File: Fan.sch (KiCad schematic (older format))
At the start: 0 parts

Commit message: Fan Schematic
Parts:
- added Q?: MOSFET_N, ~, symbol MOSFET_N
- added R? (x5): R, ~, symbol R
- added RV?: POT, ~, symbol POT
- added U?: LM324, ~, symbol LM324
- added U?: MCP4922-E/P, DIP14, symbol MCP4922-E/P
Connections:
- net labels added: +12V, -12V, AGND, CS_N, Current Measure, MISO, MOSI, SCLK
- wire segments 0 -> 35

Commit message: Overall Schematic
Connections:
- net labels added: CURR_MEAS, FAN_EN_N, FAN_OUT+, FAN_OUT-, TACH_IN, TACH_MEAS
- net labels removed: Current Measure, Fan_In, Power+, Power-, Tach, Tach_Out
- wire segments 35 -> 43
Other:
- moved on the sheet: R?
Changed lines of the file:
@@
 $Descr A4 11693 8268
 encoding utf-8
-Sheet 7 9
+Sheet 5 9
 Title ""
-Date "22 sep 2013"
+Date "28 sep 2013"
 Rev ""
 Comp ""
@@
 $EndDescr
 Text HLabel 2550 2950 0    60   Input ~ 0
-Fan_In
+FAN_EN_N
 Text HLabel 2550 3200 0    60   Output ~ 0
-Tach_Out
+TACH_MEAS
 Text HLabel 8950 2450 0    60   Output ~ 0
-Power+
-Text HLabel 8950 2650 0    60   Input ~ 0
-Power-
+FAN_OUT+
+Text HLabel 8950 2650 0    60   Output ~ 0
+FAN_OUT-
 Text HLabel 8950 2850 0    60   Input ~ 0
-Tach
+TACH_IN
 $Comp
 L LM324 U?
@@
 	8950 2650 7600 2650
 Wire Wire Line
-	7600 2650 7600 3300
+	7600 2650 7600 3200
+Wire Wire Line
+	7600 3200 7600 3300
 $Comp
 L R R?
@@
 	5950 2850 5950 2550
 Wire Wire Line
-	3500 3200 7600 3200
+	3500 3200 5350 3200
+Wire Wire Line
+	5350 3200 7600 3200
 Wire Wire Line
 	5350 3200 5350 2250
@@
 	7600 1950 7600 1550
 Wire Wire Line
-	4200 2050 5550 2050
+	4250 2050 4700 2050
+Wire Wire Line
+	4700 2050 5550 2050
 $Comp
 L +12V #PWR?
@@
 	4250 1500 4250 1250
 Wire Wire Line
-	4250 2000 4250 2300
+	4250 2000 4250 2050
+Wire Wire Line
+	4250 2050 4250 2150
+Wire Wire Line
+	4250 2150 4250 2300
 $Comp
 L POT RV?
@@
 Wire Wire Line
 	3150 3200 2550 3200
-Text HLabel 2850 3100 0    60   Output ~ 0
-Current Measure
+Text HLabel 2600 3100 0    60   Output ~ 0
+CURR_MEAS
 Wire Wire Line
 	3500 3200 3500 3100
 Wire Wire Line
-	3500 3100 2850 3100
+	3500 3100 2600 3100
 Connection ~ 5350 3200
 Wire Wire Line
-	2550 2950 3600 2950
+	2550 2950 2850 2950
+Wire Wire Line
+	2850 2950 3600 2950
 Wire Wire Line
 	3600 2950 3600 3150
@@
 L R R?
 U 1 1 523BCB9D
-P 3950 2050
-F 0 "R?" V 4030 2050 40  0000 C CNN
-F 1 "R" V 3957 2051 40  0000 C CNN
-F 2 "~" V 3880 2050 30  0000 C CNN
-F 3 "~" H 3950 2050 30  0000 C CNN
-	1    3950 2050
+P 3900 2100
+F 0 "R?" V 3980 2100 40  0000 C CNN
+F 1 "R" V 3907 2101 40  0000 C CNN
+F 2 "~" V 3830 2100 30  0000 C CNN
+F 3 "~" H 3900 2100 30  0000 C CNN
+	1    3900 2100
 	0    -1   -1   0
 $EndComp
 Wire Wire Line
-	3650 2050 3700 2050
+	3650 2050 3650 2100
 Text HLabel 2200 2000 0    60   Input ~ 0
 MOSI
@@
 	2850 2750 2850 2950
 Connection ~ 2850 2950
+Wire Wire Line
+	4150 2150 4250 2150
+Wire Wire Line
+	4150 2150 4150 2100
+Connection ~ 4250 2150
 $EndSCHEMATC

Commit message: Fan/Current Module Refactoring
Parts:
- removed R? (x3): R, ~, symbol R
- removed RV?: POT, ~, symbol POT
- added D?: DIODE, ~, symbol DIODE
- added Q? (x2): MOSFET_N, ~, symbol MOSFET_N
- added TH?: THERMISTOR, ~, symbol THERMISTOR
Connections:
- net labels added: +12C, FAN_MODE, FAN_PWM
- net labels removed: FAN_EN_N
- wire segments 43 -> 30
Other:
- moved on the sheet: R?
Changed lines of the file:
@@
 Sheet 5 9
 Title ""
-Date "28 sep 2013"
+Date "30 sep 2013"
 Rev ""
 Comp ""
@@
 Comment4 ""
 $EndDescr
-Text HLabel 2550 2950 0    60   Input ~ 0
-FAN_EN_N
-Text HLabel 2550 3200 0    60   Output ~ 0
+Text HLabel 2600 2950 0    60   Input ~ 0
+FAN_PWM
+Text HLabel 2600 4450 0    60   Output ~ 0
 TACH_MEAS
-Text HLabel 8950 2450 0    60   Output ~ 0
+Text HLabel 9300 1450 2    60   Output ~ 0
 FAN_OUT+
-Text HLabel 8950 2650 0    60   Output ~ 0
+Text HLabel 9300 1650 2    60   Output ~ 0
 FAN_OUT-
-Text HLabel 8950 2850 0    60   Input ~ 0
+Text HLabel 9250 4450 2    60   Input ~ 0
 TACH_IN
 $Comp
@@
 	1    0    0    -1
 $EndComp
-$Comp
-L +12V #PWR?
-U 1 1 523BC5F8
-P 7600 1600
-F 0 "#PWR?" H 7600 1550 20  0001 C CNN
-F 1 "+12V" H 7600 1700 30  0000 C CNN
-F 2 "" H 7600 1600 60  0000 C CNN
-F 3 "" H 7600 1600 60  0000 C CNN
-	1    7600 1600
-	1    0    0    -1
-$EndComp
 Wire Wire Line
 	6550 2150 7300 2150
 Wire Wire Line
-	7600 2350 7600 2450
-Wire Wire Line
-	7600 2450 8950 2450
-Wire Wire Line
-	8950 2650 7600 2650
-Wire Wire Line
-	7600 2650 7600 3200
-Wire Wire Line
-	7600 3200 7600 3300
+	7600 2350 7600 3450
 $Comp
 L R R?
 U 1 1 523BC667
-P 7600 3550
-F 0 "R?" V 7680 3550 40  0000 C CNN
-F 1 "R" V 7607 3551 40  0000 C CNN
-F 2 "~" V 7530 3550 30  0000 C CNN
-F 3 "~" H 7600 3550 30  0000 C CNN
-	1    7600 3550
+P 7600 3700
+F 0 "R?" V 7680 3700 40  0000 C CNN
+F 1 "R" V 7607 3701 40  0000 C CNN
+F 2 "~" V 7530 3700 30  0000 C CNN
+F 3 "~" H 7600 3700 30  0000 C CNN
+	1    7600 3700
 	1    0    0    -1
 $EndComp
@@
 L AGND #PWR?
 U 1 1 523BC6A2
-P 7600 4050
-F 0 "#PWR?" H 7600 4050 40  0001 C CNN
-F 1 "AGND" H 7600 3980 50  0000 C CNN
-F 2 "" H 7600 4050 60  0000 C CNN
-F 3 "" H 7600 4050 60  0000 C CNN
-	1    7600 4050
-	1    0    0    -1
-$EndComp
-Wire Wire Line
-	7600 3800 7600 4050
+P 7600 4250
+F 0 "#PWR?" H 7600 4250 40  0001 C CNN
+F 1 "AGND" H 7600 4180 50  0000 C CNN
+F 2 "" H 7600 4250 60  0000 C CNN
+F 3 "" H 7600 4250 60  0000 C CNN
+	1    7600 4250
+	1    0    0    -1
+$EndComp
+Wire Wire Line
+	7600 3950 7600 4250
 $Comp
 L +12V #PWR?
@@
 	5950 2850 5950 2550
 Wire Wire Line
-	3500 3200 5350 3200
-Wire Wire Line
-	5350 3200 7600 3200
+	2600 3200 7600 3200
 Wire Wire Line
 	5350 3200 5350 2250
@@
 Connection ~ 7600 3200
 Wire Wire Line
-	7600 1950 7600 1550
-Wire Wire Line
-	4250 2050 4700 2050
-Wire Wire Line
-	4700 2050 5550 2050
-$Comp
-L +12V #PWR?
-U 1 1 523BC77F
-P 4250 1250
-F 0 "#PWR?" H 4250 1200 20  0001 C CNN
-F 1 "+12V" H 4250 1350 30  0000 C CNN
-F 2 "" H 4250 1250 60  0000 C CNN
-F 3 "" H 4250 1250 60  0000 C CNN
-	1    4250 1250
-	1    0    0    -1
-$EndComp
-$Comp
-L R R?
-U 1 1 523BC78E
-P 4250 1750
-F 0 "R?" V 4330 1750 40  0000 C CNN
-F 1 "R" V 4257 1751 40  0000 C CNN
-F 2 "~" V 4180 1750 30  0000 C CNN
-F 3 "~" H 4250 1750 30  0000 C CNN
-	1    4250 1750
-	1    0    0    -1
-$EndComp
-Wire Wire Line
-	4250 1500 4250 1250
-Wire Wire Line
-	4250 2000 4250 2050
-Wire Wire Line
-	4250 2050 4250 2150
-Wire Wire Line
-	4250 2150 4250 2300
-$Comp
-L POT RV?
-U 1 1 523BC7D3
-P 4250 2550
-F 0 "RV?" H 4250 2450 50  0000 C CNN
-F 1 "POT" H 4250 2550 50  0000 C CNN
-F 2 "~" H 4250 2550 60  0000 C CNN
-F 3 "~" H 4250 2550 60  0000 C CNN
-	1    4250 2550
-	0    -1   -1   0
-$EndComp
-Connection ~ 4250 2050
-Wire Wire Line
-	4250 2950 4250 2800
+	4150 2050 5550 2050
+Wire Wire Line
+	4250 2750 4250 2950
 $Comp
 L AGND #PWR?
@@
 	1    0    0    -1
 $EndComp
-Wire Wire Line
-	8950 2850 8250 2850
-Wire Wire Line
-	8250 2850 8250 4200
-Wire Wire Line
-	8250 4200 3150 4200
-Wire Wire Line
-	3150 4200 3150 3200
-Wire Wire Line
-	3150 3200 2550 3200
-Text HLabel 2600 3100 0    60   Output ~ 0
+Text HLabel 2600 3200 0    60   Output ~ 0
 CURR_MEAS
-Wire Wire Line
-	3500 3200 3500 3100
-Wire Wire Line
-	3500 3100 2600 3100
 Connection ~ 5350 3200
 Wire Wire Line
-	2550 2950 2850 2950
-Wire Wire Line
-	2850 2950 3600 2950
-Wire Wire Line
-	3600 2950 3600 3150
-Wire Wire Line
-	3600 3150 4700 3150
-Connection ~ 4700 2050
-$Comp
-L R R?
-U 1 1 523BCA8F
-P 4700 2550
-F 0 "R?" V 4780 2550 40  0000 C CNN
-F 1 "R" V 4707 2551 40  0000 C CNN
-F 2 "~" V 4630 2550 30  0000 C CNN
-F 3 "~" H 4700 2550 30  0000 C CNN
-	1    4700 2550
-	1    0    0    -1
-$EndComp
-Wire Wire Line
-	4700 3150 4700 2800
-Wire Wire Line
-	4700 2300 4700 2050
+	2600 2950 3600 2950
 $Comp
 L R R?
 U 1 1 523BCB9D
-P 3900 2100
-F 0 "R?" V 3980 2100 40  0000 C CNN
-F 1 "R" V 3907 2101 40  0000 C CNN
-F 2 "~" V 3830 2100 30  0000 C CNN
-F 3 "~" H 3900 2100 30  0000 C CNN
-	1    3900 2100
+P 3900 2050
+F 0 "R?" V 3980 2050 40  0000 C CNN
+F 1 "R" V 3907 2051 40  0000 C CNN
+F 2 "~" V 3830 2050 30  0000 C CNN
+F 3 "~" H 3900 2050 30  0000 C CNN
+	1    3900 2050
 	0    -1   -1   0
 $EndComp
 Wire Wire Line
-	3650 2050 3650 2100
+	3650 2050 3650 2050
 Text HLabel 2200 2000 0    60   Input ~ 0
 MOSI
-Text HLabel 1850 2600 0    60   Output ~ 0
+Text HLabel 2200 2300 0    60   Input ~ 0
 MISO
 Text HLabel 2200 2200 0    60   Input ~ 0
@@
 	2200 2200 2550 2200
 $Comp
-L R R?
-U 1 1 523BCC50
-P 2600 2750
-F 0 "R?" V 2680 2750 40  0000 C CNN
-F 1 "R" V 2607 2751 40  0000 C CNN
-F 2 "~" V 2530 2750 30  0000 C CNN
-F 3 "~" H 2600 2750 30  0000 C CNN
-	1    2600 2750
+L MOSFET_N Q?
+U 1 1 52492E73
+P 7250 3550
+F 0 "Q?" H 7260 3720 60  0000 R CNN
+F 1 "MOSFET_N" H 7260 3400 60  0000 R CNN
+F 2 "~" H 7250 3550 60  0000 C CNN
+F 3 "~" H 7250 3550 60  0000 C CNN
+	1    7250 3550
+	1    0    0    -1
+$EndComp
+$Comp
+L THERMISTOR TH?
+U 1 1 52492EAB
+P 7600 1150
+F 0 "TH?" V 7700 1200 50  0000 C CNN
+F 1 "THERMISTOR" V 7500 1150 50  0000 C CNN
+F 2 "~" H 7600 1150 60  0000 C CNN
+F 3 "~" H 7600 1150 60  0000 C CNN
+	1    7600 1150
+	1    0    0    -1
+$EndComp
+Wire Wire Line
+	7600 750  7600 900
+Wire Wire Line
+	7600 1400 7600 1450
+Wire Wire Line
+	7400 1450 9300 1450
+Wire Wire Line
+	9300 1650 7600 1650
+Wire Wire Line
+	7600 1650 7600 1950
+$Comp
+L DIODE D?
+U 1 1 52492FCD
+P 7200 1550
+F 0 "D?" H 7200 1650 40  0000 C CNN
+F 1 "DIODE" H 7200 1450 40  0000 C CNN
+F 2 "~" H 7200 1550 60  0000 C CNN
+F 3 "~" H 7200 1550 60  0000 C CNN
+	1    7200 1550
 	0    -1   -1   0
 $EndComp
 Wire Wire Line
-	2550 2400 2300 2400
-Wire Wire Line
-	2300 2400 2300 2750
-Wire Wire Line
-	2300 2750 2350 2750
-Wire Wire Line
-	2850 2750 2850 2950
-Connection ~ 2850 2950
-Wire Wire Line
-	4150 2150 4250 2150
-Wire Wire Line
-	4150 2150 4150 2100
-Connection ~ 4250 2150
+	7200 1350 7400 1350
+Wire Wire Line
+	7400 1350 7400 1450
+Connection ~ 7600 1450
+Wire Wire Line
+	7200 1750 7600 1750
+Connection ~ 7600 1750
+Wire Wire Line
+	7350 3350 7350 3200
+Connection ~ 7350 3200
+Wire Wire Line
+	7350 3750 7350 4050
+Wire Wire Line
+	7350 4050 7600 4050
+Connection ~ 7600 4050
+Wire Wire Line
+	2600 4450 9250 4450
+$Comp
+L MOSFET_N Q?
+U 1 1 52493547
+P 4150 2550
+F 0 "Q?" H 4160 2720 60  0000 R CNN
+F 1 "MOSFET_N" H 4160 2400 60  0000 R CNN
+F 2 "~" H 4150 2550 60  0000 C CNN
+F 3 "~" H 4150 2550 60  0000 C CNN
+	1    4150 2550
+	1    0    0    -1
+$EndComp
+Wire Wire Line
+	4250 2350 4250 2050
+Connection ~ 4250 2050
+Wire Wire Line
+	3600 2950 3600 2550
+Wire Wire Line
+	3600 2550 3950 2550
+Text HLabel 2600 3550 0    60   Input ~ 0
+FAN_MODE
+Wire Wire Line
+	7050 3550 2600 3550
+$Comp
+L +12C #PWR?
+U 1 1 52493C3F
+P 7600 750
+F 0 "#PWR?" H 7600 720 30  0001 C CNN
+F 1 "+12C" H 7600 860 40  0000 C CNN
+F 2 "" H 7600 750 60  0000 C CNN
+F 3 "" H 7600 750 60  0000 C CNN
+	1    7600 750
+	1    0    0    -1
+$EndComp
 $EndSCHEMATC

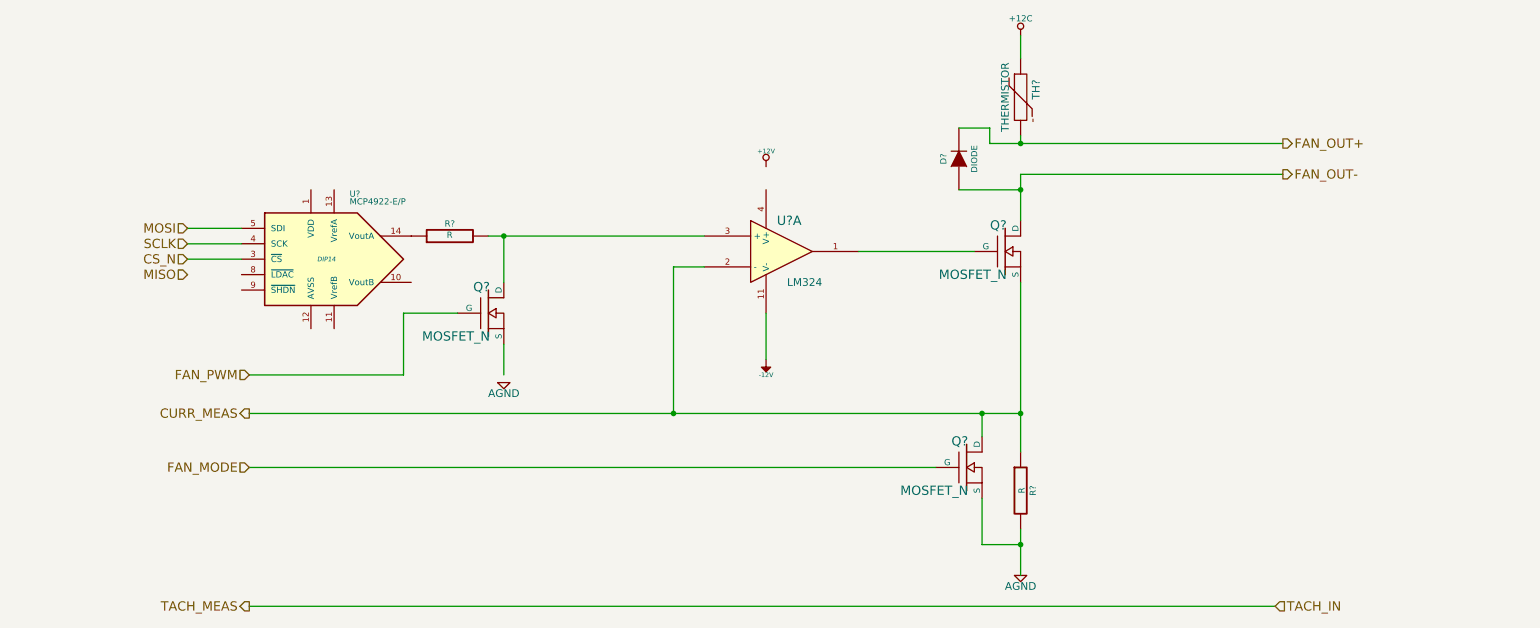
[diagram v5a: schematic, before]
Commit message: Preliminary Module Layouts
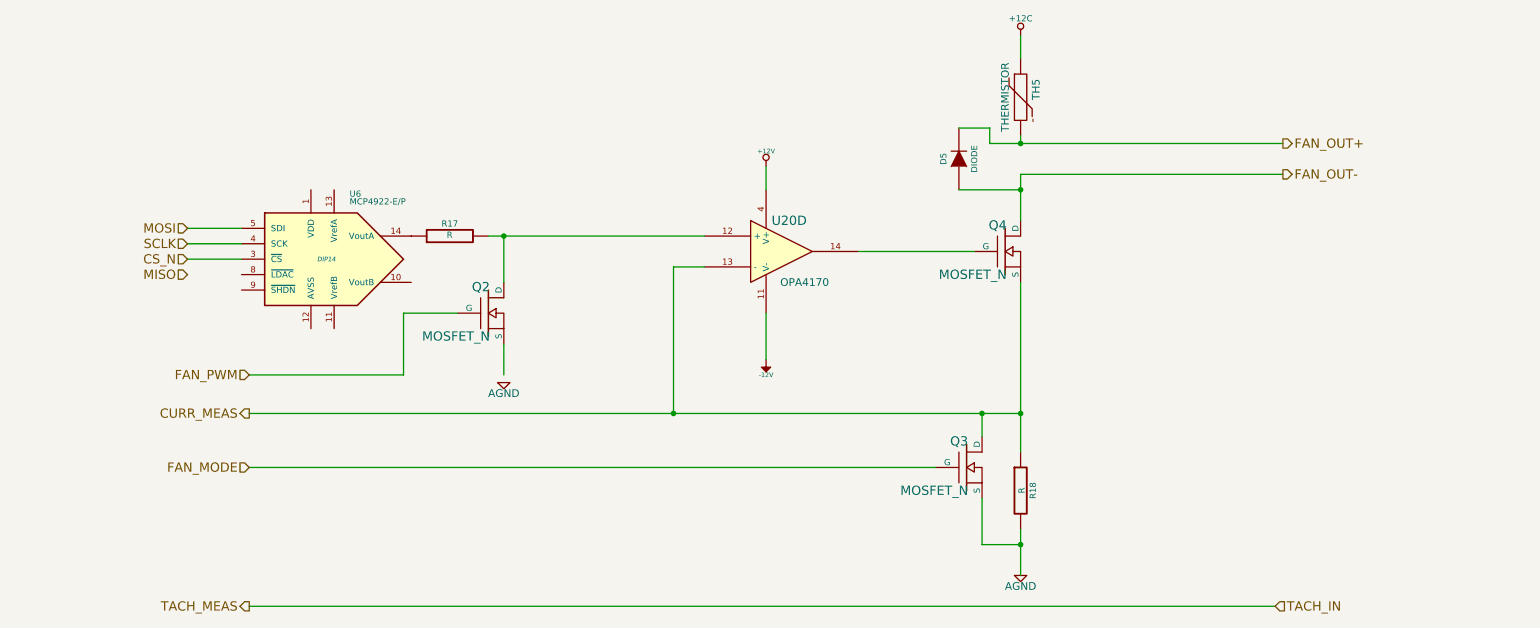
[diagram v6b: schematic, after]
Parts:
- U20: renamed from U?; value LM324 -> OPA4170
- gave numbers to parts that had none: 8
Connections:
- net +12V: now also U20.4 (V+)
- net CURR_MEAS: now also U20.13 (-); no longer U20.2 (-)
- net at Q4.1 (G): now also U20.14; no longer U20.1
- net at Q2.2 (D), R17.2: now also U20.12 (+); no longer U20.3 (+)
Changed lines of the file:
@@
 Sheet 5 9
 Title ""
-Date "30 sep 2013"
+Date "15 oct 2013"
 Rev ""
 Comp ""
@@
 TACH_IN
 $Comp
-L LM324 U?
-U 1 1 523BC5AD
+L LM324 U20
+U 4 1 523BC5AD
 P 6050 2150
-F 0 "U?" H 6100 2350 60  0000 C CNN
-F 1 "LM324" H 6200 1950 50  0000 C CNN
+F 0 "U20" H 6100 2350 60  0000 C CNN
+F 1 "OPA4170" H 6200 1950 50  0000 C CNN
 F 2 "~" H 6050 2150 60  0000 C CNN
 F 3 "~" H 6050 2150 60  0000 C CNN
-	1    6050 2150
-	1    0    0    -1
-$EndComp
-$Comp
-L MOSFET_N Q?
+	4    6050 2150
+	1    0    0    -1
+$EndComp
+$Comp
+L MOSFET_N Q4
 U 1 1 523BC5BC
 P 7500 2150
-F 0 "Q?" H 7510 2320 60  0000 R CNN
+F 0 "Q4" H 7510 2320 60  0000 R CNN
 F 1 "MOSFET_N" H 7510 2000 60  0000 R CNN
 F 2 "~" H 7500 2150 60  0000 C CNN
@@
 	7600 2350 7600 3450
 $Comp
-L R R?
+L R R18
 U 1 1 523BC667
 P 7600 3700
-F 0 "R?" V 7680 3700 40  0000 C CNN
+F 0 "R18" V 7680 3700 40  0000 C CNN
 F 1 "R" V 7607 3701 40  0000 C CNN
 F 2 "~" V 7530 3700 30  0000 C CNN
@@
 $EndComp
 $Comp
-L AGND #PWR?
+L AGND #PWR036
 U 1 1 523BC6A2
 P 7600 4250
-F 0 "#PWR?" H 7600 4250 40  0001 C CNN
+F 0 "#PWR036" H 7600 4250 40  0001 C CNN
 F 1 "AGND" H 7600 4180 50  0000 C CNN
 F 2 "" H 7600 4250 60  0000 C CNN
@@
 	7600 3950 7600 4250
 $Comp
-L +12V #PWR?
+L +12V #PWR037
 U 1 1 523BC6C6
 P 5950 1600
-F 0 "#PWR?" H 5950 1550 20  0001 C CNN
+F 0 "#PWR037" H 5950 1550 20  0001 C CNN
 F 1 "+12V" H 5950 1700 30  0000 C CNN
 F 2 "" H 5950 1600 60  0000 C CNN
@@
 $EndComp
 $Comp
-L -12V #PWR?
+L -12V #PWR038
 U 1 1 523BC6E4
 P 5950 2850
-F 0 "#PWR?" H 5950 2980 20  0001 C CNN
+F 0 "#PWR038" H 5950 2980 20  0001 C CNN
 F 1 "-12V" H 5950 2950 30  0000 C CNN
 F 2 "" H 5950 2850 60  0000 C CNN
@@
 	4250 2750 4250 2950
 $Comp
-L AGND #PWR?
+L AGND #PWR039
 U 1 1 523BC839
 P 4250 3000
-F 0 "#PWR?" H 4250 3000 40  0001 C CNN
+F 0 "#PWR039" H 4250 3000 40  0001 C CNN
 F 1 "AGND" H 4250 2930 50  0000 C CNN
 F 2 "" H 4250 3000 60  0000 C CNN
@@
 $EndComp
 $Comp
-L MCP4922-E/P U?
+L MCP4922-E/P U6
 U 1 1 523BC8D3
 P 3100 2200
-F 0 "U?" H 3250 2600 40  0000 L BNN
+F 0 "U6" H 3250 2600 40  0000 L BNN
 F 1 "MCP4922-E/P" H 3250 2550 40  0000 L BNN
 F 2 "DIP14" H 3100 2200 30  0000 C CIN
@@
 	2600 2950 3600 2950
 $Comp
-L R R?
+L R R17
 U 1 1 523BCB9D
 P 3900 2050
-F 0 "R?" V 3980 2050 40  0000 C CNN
+F 0 "R17" V 3980 2050 40  0000 C CNN
 F 1 "R" V 3907 2051 40  0000 C CNN
 F 2 "~" V 3830 2050 30  0000 C CNN
@@
 	2200 2200 2550 2200
 $Comp
-L MOSFET_N Q?
+L MOSFET_N Q3
 U 1 1 52492E73
 P 7250 3550
-F 0 "Q?" H 7260 3720 60  0000 R CNN
+F 0 "Q3" H 7260 3720 60  0000 R CNN
 F 1 "MOSFET_N" H 7260 3400 60  0000 R CNN
 F 2 "~" H 7250 3550 60  0000 C CNN
@@
 $EndComp
 $Comp
-L THERMISTOR TH?
+L THERMISTOR TH5
 U 1 1 52492EAB
 P 7600 1150
-F 0 "TH?" V 7700 1200 50  0000 C CNN
+F 0 "TH5" V 7700 1200 50  0000 C CNN
 F 1 "THERMISTOR" V 7500 1150 50  0000 C CNN
 F 2 "~" H 7600 1150 60  0000 C CNN
@@
 	7600 1650 7600 1950
 $Comp
-L DIODE D?
+L DIODE D5
 U 1 1 52492FCD
 P 7200 1550
-F 0 "D?" H 7200 1650 40  0000 C CNN
+F 0 "D5" H 7200 1650 40  0000 C CNN
 F 1 "DIODE" H 7200 1450 40  0000 C CNN
 F 2 "~" H 7200 1550 60  0000 C CNN
@@
 	2600 4450 9250 4450
 $Comp
-L MOSFET_N Q?
+L MOSFET_N Q2
 U 1 1 52493547
 P 4150 2550
-F 0 "Q?" H 4160 2720 60  0000 R CNN
+F 0 "Q2" H 4160 2720 60  0000 R CNN
 F 1 "MOSFET_N" H 4160 2400 60  0000 R CNN
 F 2 "~" H 4150 2550 60  0000 C CNN
@@
 	7050 3550 2600 3550
 $Comp
-L +12C #PWR?
+L +12C #PWR040
 U 1 1 52493C3F
 P 7600 750
-F 0 "#PWR?" H 7600 720 30  0001 C CNN
+F 0 "#PWR040" H 7600 720 30  0001 C CNN
 F 1 "+12C" H 7600 860 40  0000 C CNN
 F 2 "" H 7600 750 60  0000 C CNN
@@
 	1    0    0    -1
 $EndComp
+Wire Wire Line
+	5950 1750 5950 1600
 $EndSCHEMATC
